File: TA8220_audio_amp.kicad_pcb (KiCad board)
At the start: 2 copper layers, 57.4 x 45.3 mm, 24 parts, among them J1 Input, J2 Output, J3 Power

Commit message: http://vicdiy.com/products/TV_linked_amp2/linked_amp2.html を参考に利得を下げるよう部品を変更
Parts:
- removed C6, C7: 25v47uF, Capacitor_THT:CP_Radial_D5.0mm_P2.50mm
- added R5: 18k, Resistor_THT:R_Axial_DIN0411_L9.9mm_D3.6mm_P15.24mm_Horizontal, F.Cu at (129.5, 56.0)
- added R6: 18k, Resistor_THT:R_Axial_DIN0411_L9.9mm_D3.6mm_P12.70mm_Horizontal, F.Cu at (123.7, 62.1)
- C8: value 1000uF -> 25v1000uF
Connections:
- C1 pad 1: Net-(U1-IN1) -> Net-(C1-Pad1)
- C2 pad 1: Net-(U1-IN2) -> Net-(C2-Pad1)
- C3 pad 1: Net-(U1-IN1) -> Net-(C1-Pad1)
- C4 pad 1: Net-(U1-IN2) -> Net-(C2-Pad1)
- U1 pad 3: Net-(U1-NF1) -> unconnected-(U1-NF1-Pad3)
- U1 pad 6: Net-(U1-NF2) -> unconnected-(U1-NF2-Pad6)
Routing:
- net unconnected-(U1-NF1-Pad3): track 0.00 -> 9.29 mm
- net Net-(U1-NF1): track 9.29 -> 0.00 mm
- net unconnected-(U1-NF2-Pad6): track 0.00 -> 8.22 mm
- net Net-(U1-NF2): track 8.22 -> 0.00 mm

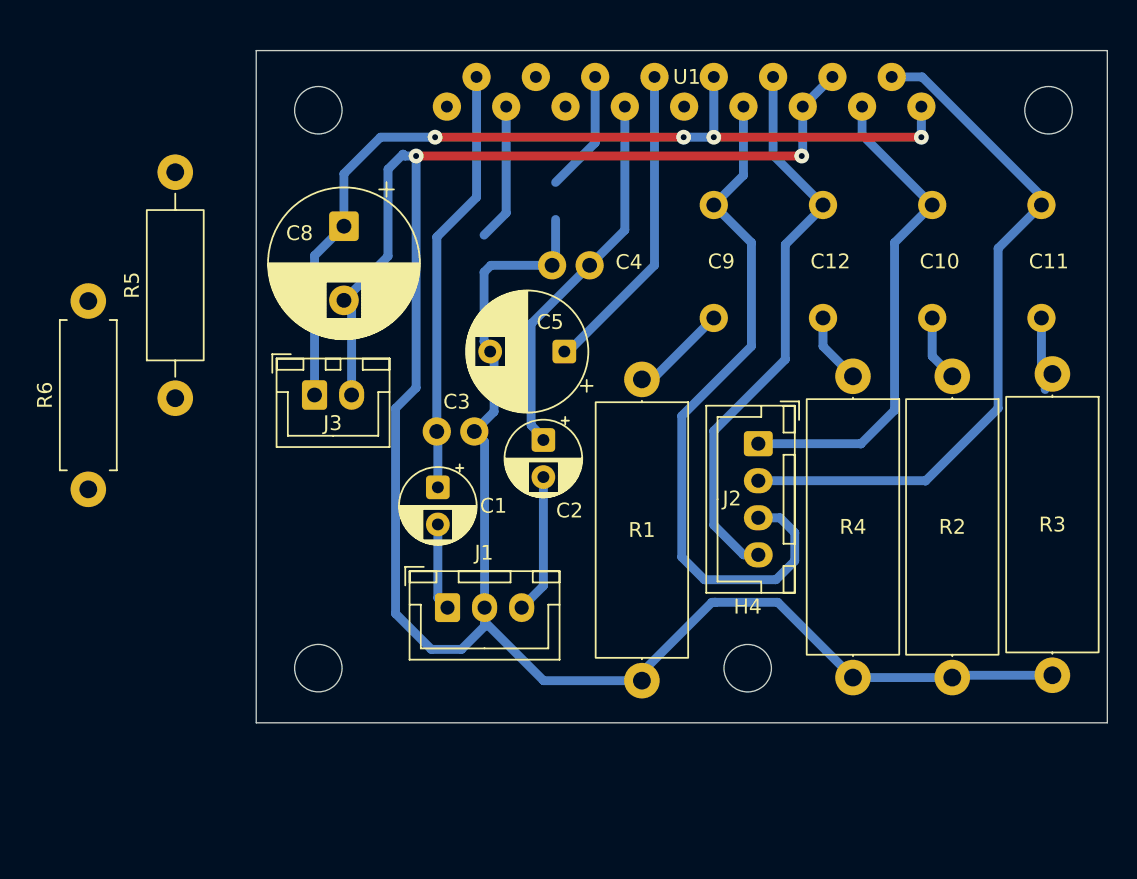
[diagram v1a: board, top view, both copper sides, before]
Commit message: パッド径を2に修正
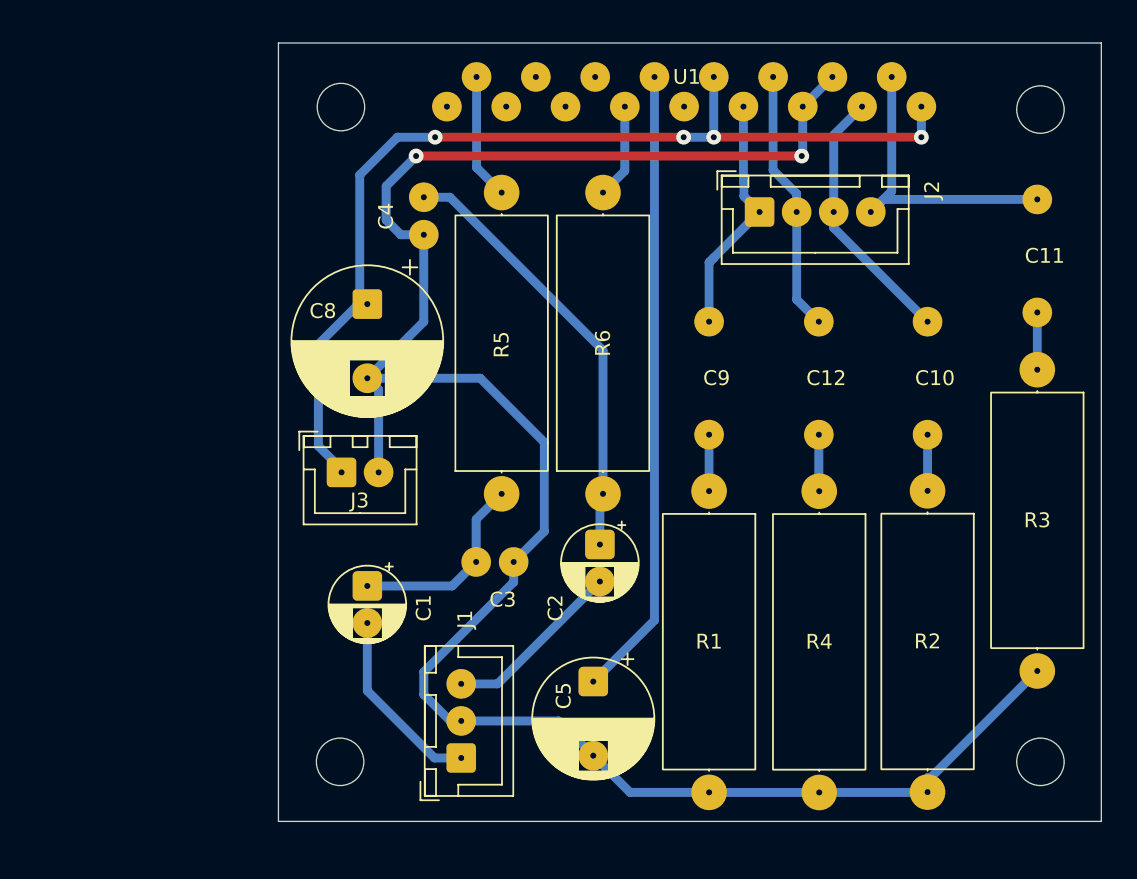
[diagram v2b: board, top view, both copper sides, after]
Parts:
- R5: footprint Resistor_THT:R_Axial_DIN0411_L9.9mm_D3.6mm_P15.24mm_Horizontal -> Resistor_THT:R_Axial_DIN0617_L17.0mm_D6.0mm_P20.32mm_Horizontal
- R6: footprint Resistor_THT:R_Axial_DIN0411_L9.9mm_D3.6mm_P12.70mm_Horizontal -> Resistor_THT:R_Axial_DIN0617_L17.0mm_D6.0mm_P20.32mm_Horizontal
- moved R6 34.7 mm to (158.4, 62.4)
- moved R5 22.9 mm to (151.6, 62.4)
- moved C5 22.3 mm to (157.7, 75.1), turned to -90 degrees
- moved H4 20.7 mm to (187.9, 80.5)
- moved J2 15.6 mm to (169.0, 43.4), turned to 0 degrees
- moved C4 10.4 mm to (146.3, 43.7), turned to -90 degrees
- moved J1 10.2 mm to (148.8, 80.2), turned to 90 degrees
- moved C3 9.19 mm to (151.1, 67.0)
- moved R1 8.79 mm to (165.5, 62.2)
- moved C1 8.18 mm to (142.5, 68.6)
- moved R4 8.08 mm to (173.0, 62.2)
- moved C2 8.01 mm to (158.2, 65.8)
- moved R2 7.90 mm to (180.3, 62.2)
- moved C10 7.88 mm to (180.3, 54.6)
- moved C12 7.88 mm to (172.9, 54.6)
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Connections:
- C10 pad 1: Net-(J2-Pin_1) -> Net-(J2-Pin_3)
- C11 pad 1: Net-(J2-Pin_2) -> Net-(J2-Pin_4)
- C12 pad 1: Net-(J2-Pin_4) -> Net-(J2-Pin_2)
- C9 pad 1: Net-(J2-Pin_3) -> Net-(J2-Pin_1)
- U1 pad 11: Net-(J2-Pin_3) -> Net-(J2-Pin_1)
- U1 pad 12: Net-(J2-Pin_4) -> Net-(J2-Pin_2)
- U1 pad 15: Net-(J2-Pin_1) -> Net-(J2-Pin_3)
- U1 pad 16: Net-(J2-Pin_2) -> Net-(J2-Pin_4)
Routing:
- net Net-(J2-Pin_3): track 47.8 -> 17.9 mm
- net Net-(C2-Pad1): track 0.00 -> 29.5 mm
- net GND: track 170.0 -> 140.6 mm
- net Net-(J2-Pin_2): track 47.2 -> 18.6 mm
- net Net-(U1-Ripple): track 20.9 -> 42.5 mm
- net Net-(U1-IN1): track 28.8 -> 8.50 mm
- net Net-(U1-IN2): track 25.5 -> 6.41 mm
- net Net-(J2-Pin_4): track 38.5 -> 21.3 mm
- net Net-(J2-Pin_1): track 33.6 -> 16.8 mm
- net Net-(C1-Pad1): track 0.00 -> 13.3 mm
- net unconnected-(U1-NF1-Pad3): track 9.29 -> 0.00 mm
- net unconnected-(U1-NF2-Pad6): track 8.22 -> 0.00 mm
- net Net-(J1-Pin_1): track 5.88 -> 12.8 mm
- net VCC: track 61.8 -> 67.5 mm
- net Net-(C11-Pad2): track 6.81 -> 3.49 mm
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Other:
- board size 57.4 x 45.3 mm -> 55.5 x 52.5 mm

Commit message: 50mmに収めた
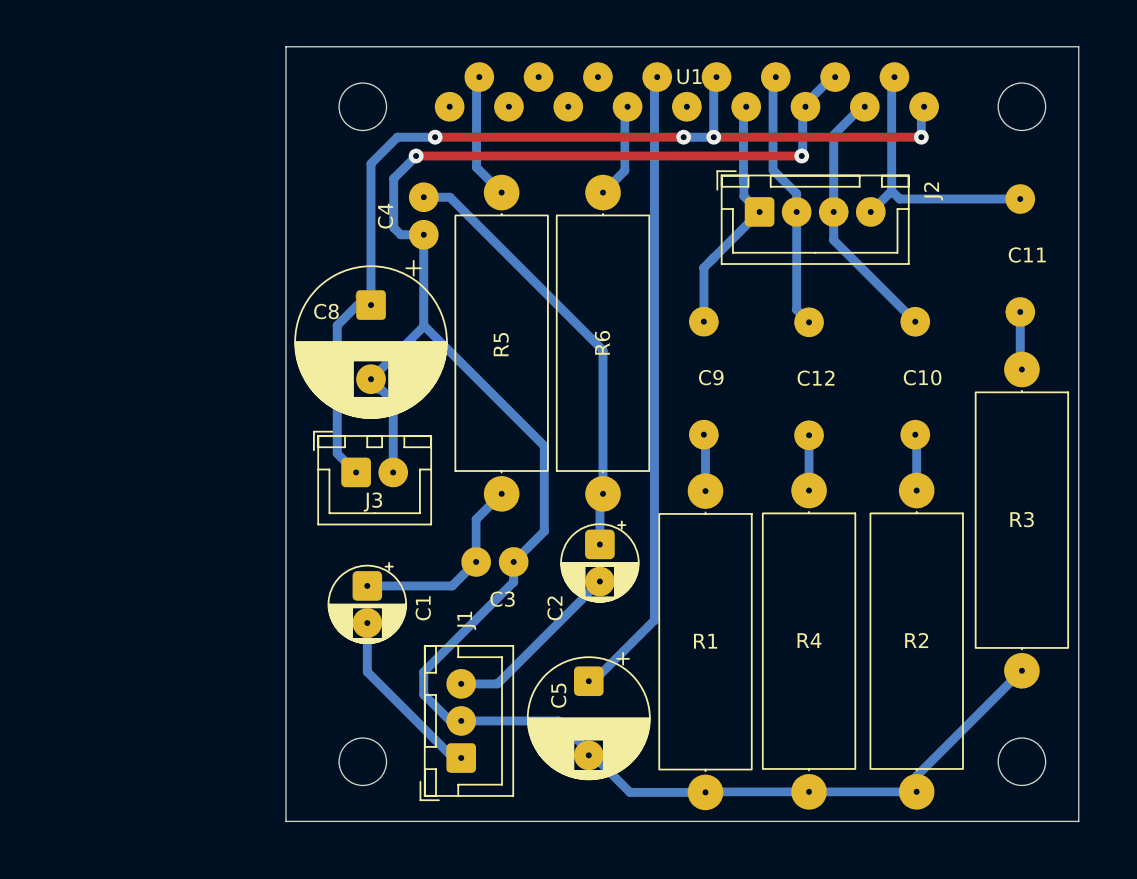
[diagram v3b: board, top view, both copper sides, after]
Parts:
- moved H3 1.53 mm to (142.2, 80.5)
- moved H1 1.47 mm to (142.2, 36.3)
- moved H2 1.26 mm to (186.6, 36.3)
- moved H4 1.25 mm to (186.6, 80.5)
- moved C11 1.15 mm to (186.5, 46.3)
- moved R3 1.04 mm to (186.6, 54.0)
- moved J3 0.98 mm to (141.7, 61.0)
- moved C10 0.83 mm to (179.5, 54.6)
- moved R2 0.73 mm to (179.5, 62.2)
- moved R4 0.69 mm to (172.3, 62.2)
- moved C12 0.66 mm to (172.3, 54.6)
- moved C9 0.35 mm to (165.2, 54.6)
- moved C5 0.30 mm to (157.4, 75.0)
- moved C8 0.26 mm to (142.7, 49.7)
- moved R1 0.24 mm to (165.3, 62.2)
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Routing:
- net Net-(J2-Pin_4): track 21.3 -> 18.6 mm
- net GND: track 140.6 -> 138.4 mm
- net Net-(J1-Pin_1): track 12.8 -> 12.0 mm
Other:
- board size 55.5 x 52.5 mm -> 53.5 x 52.2 mm

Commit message: パッド修正、ベタ追加
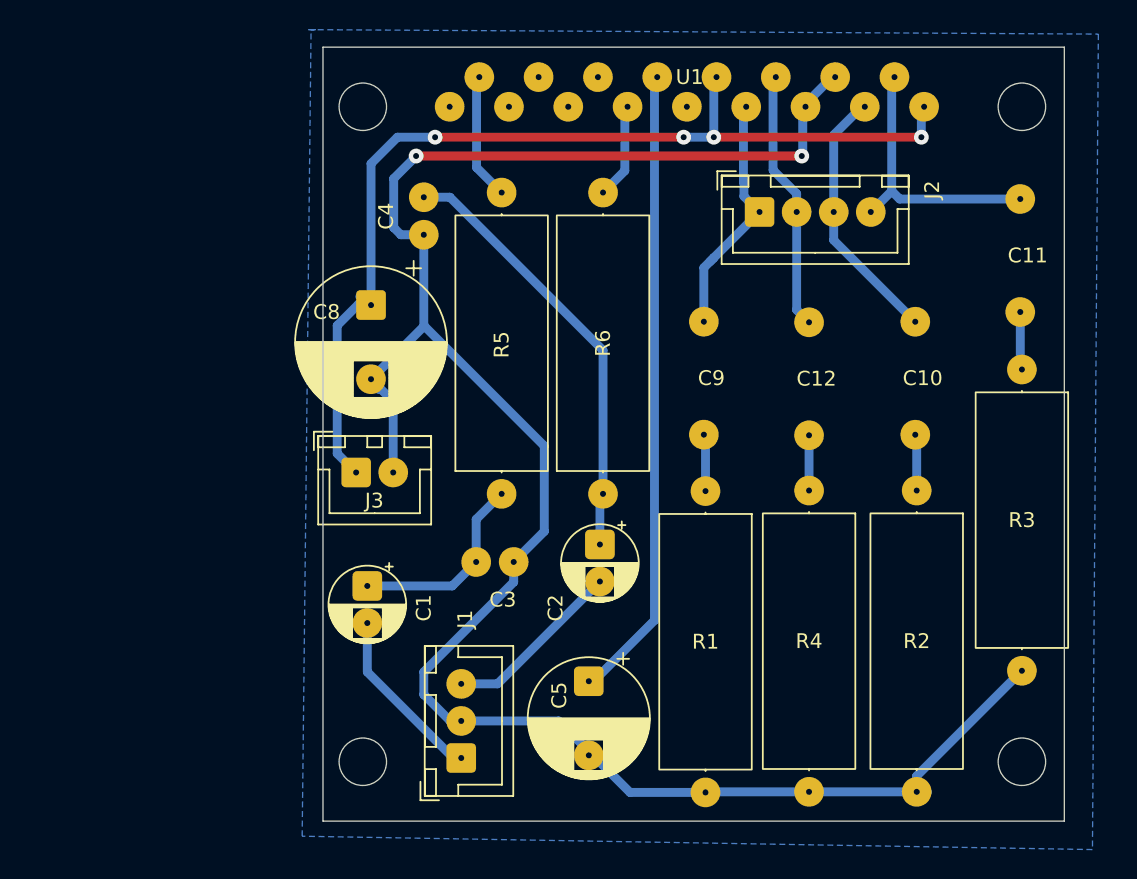
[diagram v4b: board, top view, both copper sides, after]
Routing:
- added copper zone on B.Cu, net (none)
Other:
- board size 53.5 x 52.2 mm -> 50 x 52.2 mm
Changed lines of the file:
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@@
 		(pad "1" thru_hole circle
 			(at 0 0 90)
-			(size 2.4 2.4)
+			(size 2 2)
 			(drill 0.4)
 			(layers "*.Cu" "*.Mask")
@@
 		(pad "2" thru_hole circle
 			(at 20.32 0 90)
-			(size 2.4 2.4)
+			(size 2 2)
 			(drill 0.4)
 			(layers "*.Cu" "*.Mask")
@@
 		(pad "1" thru_hole circle
 			(at 0 0 270)
-			(size 2.4 2.4)
+			(size 2 2)
 			(drill 0.4)
 			(layers "*.Cu" "*.Mask")
@@
 		(pad "2" thru_hole circle
 			(at 20.32 0 270)
-			(size 2.4 2.4)
+			(size 2 2)
 			(drill 0.4)
 			(layers "*.Cu" "*.Mask")
@@
 		(pad "1" thru_hole circle
 			(at 0 0 270)
-			(size 2.4 2.4)
+			(size 2 2)
 			(drill 0.4)
 			(layers "*.Cu" "*.Mask")
@@
 		(pad "2" thru_hole circle
 			(at 20.32 0 270)
-			(size 2.4 2.4)
+			(size 2 2)
 			(drill 0.4)
 			(layers "*.Cu" "*.Mask")
@@
 		(pad "1" thru_hole circle
 			(at 0 0 90)
-			(size 2.4 2.4)
+			(size 2 2)
 			(drill 0.4)
 			(layers "*.Cu" "*.Mask")
@@
 		(pad "2" thru_hole circle
 			(at 20.32 0 90)
-			(size 2.4 2.4)
+			(size 2 2)
 			(drill 0.4)
 			(layers "*.Cu" "*.Mask")
@@
 		(pad "1" thru_hole circle
 			(at 0 0 270)
-			(size 2.4 2.4)
+			(size 2 2)
 			(drill 0.4)
 			(layers "*.Cu" "*.Mask")
@@
 		(pad "2" thru_hole circle
 			(at 20.32 0 270)
-			(size 2.4 2.4)
+			(size 2 2)
 			(drill 0.4)
 			(layers "*.Cu" "*.Mask")
@@
 		(pad "1" thru_hole circle
 			(at 0 0 270)
-			(size 2.4 2.4)
+			(size 2 2)
 			(drill 0.4)
 			(layers "*.Cu" "*.Mask")
@@
 		(pad "2" thru_hole circle
 			(at 20.32 0 270)
-			(size 2.4 2.4)
+			(size 2 2)
 			(drill 0.4)
 			(layers "*.Cu" "*.Mask")
@@
 	)
 	(gr_rect
-		(start 137.008 32.254)
-		(end 190.476 84.5)
+		(start 139.504172 32.280413)
+		(end 189.504172 84.480413)
 		(stroke
 			(width 0.05)
@@
 		(net 21)
 	)
+	(zone
+		(net 0)
+		(net_name "")
+		(layer "B.Cu")
+		(hatch edge 0.5)
+		(connect_pads
+			(clearance 0.8)
+		)
+		(min_thickness 0.25)
+		(filled_areas_thickness no)
+		(fill yes
+			(thermal_gap 0.5)
+			(thermal_bridge_width 0.5)
+			(island_removal_mode 1)
+			(island_area_min 10)
+		)
+		(polygon
+			(pts
+				(xy 138.5 31.1) (xy 191.8 31.4) (xy 191.4 86.4) (xy 138.1 85.5) (xy 138.7 31.1) (xy 139 31.1)
+			)
+		)
+	)
 	(embedded_fonts no)
